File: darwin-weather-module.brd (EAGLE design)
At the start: 85 x 25 mm, 16 parts, among them J1 2X6-HEADERS, J2 95501-6889VERT, U1 P82B715SOIC, U2 ATSAMD09, U3 M24C02-WMN6TP

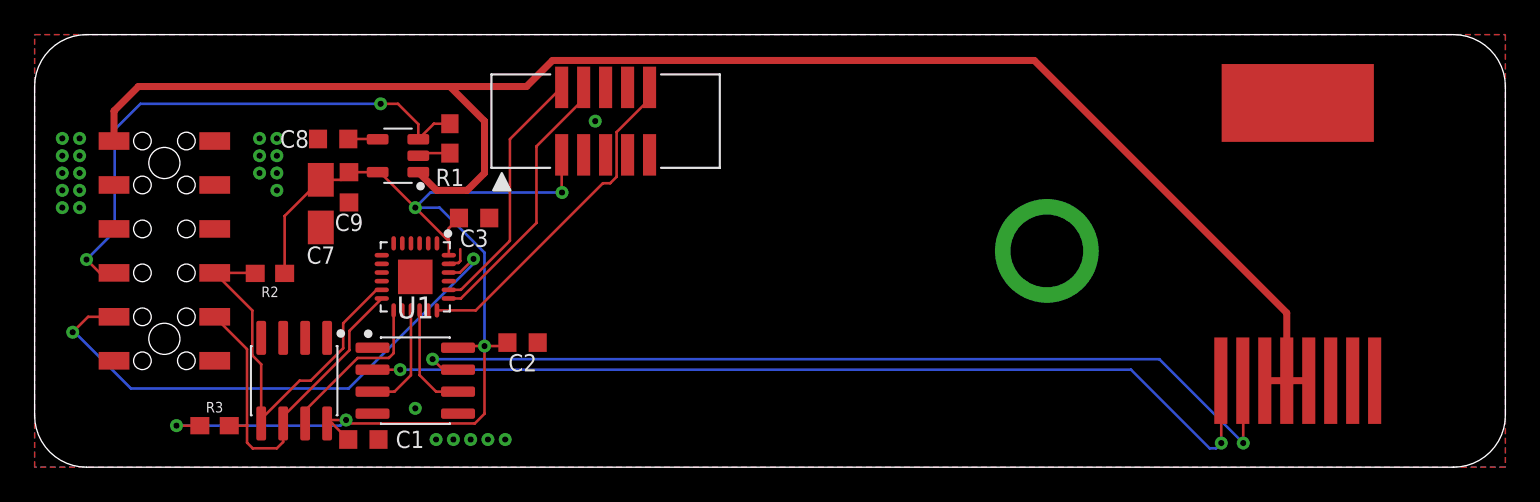
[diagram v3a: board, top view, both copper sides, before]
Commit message: Changed range extender to PCA9615
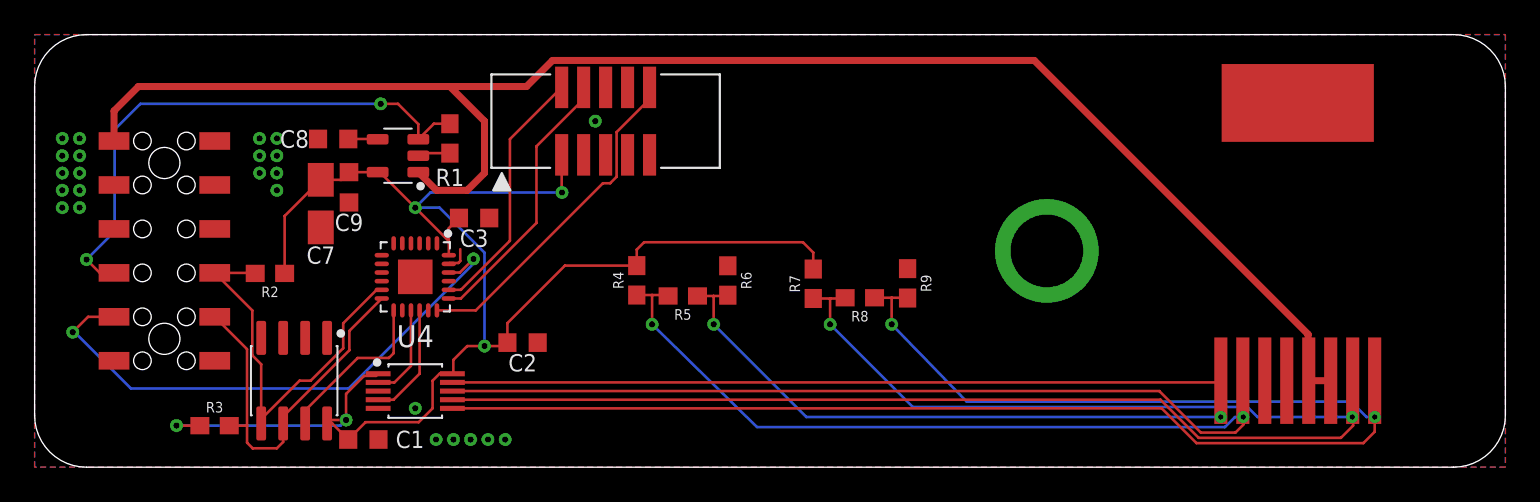
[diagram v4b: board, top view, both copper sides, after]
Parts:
- removed U1: P82B715SOIC, Conservify:SOIC127P599X175-8
- added R4, R7: 330, SparkFun-Resistors:0603
- added R5, R8: 100, SparkFun-Resistors:0603
- added R6, R9: 300, SparkFun-Resistors:0603
- added U4: PCA9615, Conservify:SOP50P490X110-10
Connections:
- removed net LCL: J2.7, U1.7
- removed net LDA: J2.8, U1.2
- new net EN: U4.3
- new net LCL-M: J2.1, R8.1, R9.2, U4.6
- new net LCL-P: J2.2, R7.1, R8.2, U4.7
- new net LDA-M: J2.8, R5.1, R6.2, U4.9
- new net LDA-P: J2.7, R4.1, R5.2, U4.8
- net 3V3: now also R4.2, R7.2, U4.1, U4.10; no longer U1.8
- net GND: now also J2.5, J2.6, R6.1, R9.1, U4.5; no longer J2.1, J2.2, J2.3, U1.4
- net SENSE-SCL: now also U4.4; no longer U1.6
- net SENSE-SDA: now also U4.2; no longer U1.3
- net UNREG: now also J2.3; no longer J2.5, J2.6
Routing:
- net LCL-P: track 0.00 -> 91.6 mm, vias 0 -> 2
- net LCL-M: track 0.00 -> 91.0 mm, vias 0 -> 2
- net LDA-P: track 0.00 -> 89.8 mm, vias 0 -> 2
- net LDA-M: track 0.00 -> 79.4 mm, vias 0 -> 2
- net LDA: track 54.7 -> 0.00 mm, vias 2 -> 0
- net LCL: track 54.2 -> 0.00 mm, vias 2 -> 0
- net 3V3: track 68.8 -> 92.8 mm
- net SENSE-SDA: track 6.36 -> 5.50 mm
- net UNREG: track 93.7 -> 93.0 mm
